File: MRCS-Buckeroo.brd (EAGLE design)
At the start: 69 x 50 mm, 11 parts

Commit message: sent to fab
sent to fab
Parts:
- removed FRAME1: FRAME-LETTER, SparkFun-Aesthetics:CREATIVE_COMMONS
- removed GND: CONNECTOR-M12LOCK, SPCoast:1X12_LOCK
- added OUTPUT-: OUTPUT-, SPCoast:1X12_LOCK
- CON1, CON2: value (none) -> DC PWR
- CON3: value (none) -> output bypass
- CON4: value (none) -> GND BYPASS
- OUTPUT+: value CONNECTOR-M12LOCK -> OUTPUT+
- moved CON3 148.8 mm to (34.3, 44.5)
- moved CON4 144.8 mm to (45.7, 12.7)
- moved U$4 91.4 mm to (35.6, 30.5)
- moved CON2 78.9 mm to (34.3, 10.2)
- moved CON1 55.5 mm to (24.1, 12.7)
- moved U$1 9.25 mm to (40.6, 36.8)
- renumbered OUTPUT to OUTPUT+
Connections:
- net N$1 renamed INPUT+
- net N$2 renamed GND
- net N$4 renamed OUTPUT+
- removed net N$3: CON4.1, GND.1, GND.10, GND.11, GND.12, GND.2, GND.3, GND.4, GND.5, GND.6, GND.7, GND.8, GND.9, U$4.OUT-
- new net OUTPUT-: CON4.1, OUTPUT-.1, OUTPUT-.10, OUTPUT-.11, OUTPUT-.12, OUTPUT-.2, OUTPUT-.3, OUTPUT-.4, OUTPUT-.5, OUTPUT-.6, OUTPUT-.7, OUTPUT-.8, OUTPUT-.9, U$4.OUT-
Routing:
- net INPUT+: track 0.00 -> 78.3 mm
- net OUTPUT-: track 0.00 -> 63.8 mm
- net GND: track 0.00 -> 57.0 mm
- net N$3: track 29.2 -> 0.00 mm
- added copper zone on layer 16, net OUTOUT-
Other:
- board text added: ""Buckeroo" Seth Neumann 20200929"
- board text added: "+ V Jumper"
- board text added: "- V (GND) JUMP"
- board text added: "IN - +"
- board text added: "Output +"
- board text added: "Output -"
- board text removed: "+12V"
- board text removed: "12V"
- board text removed: "CON4"
- board text removed: "Power & Ground Distribution"
- board text removed: "ULK"
- board text removed: "ULK GND +12"
- board text removed: "UnLock"

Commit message: Added 1st pass of documentation
Assembly and Installation Instructions
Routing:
- net OUTPUT-: track 63.8 -> 93.0 mm
- net INPUT+: track 78.3 -> 71.0 mm
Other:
- board text added: ""Buckeroo V1.2" Seth Neumann 20201120"
- board text removed: ""Buckeroo" Seth Neumann 20200929"

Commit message: Added regulator options
Supports MH-Mini-360 bucking converter and 780X TO-220 linear regulators
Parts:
- added C1: 150uF@50, SPCoast:E5-10.5
- added C2: 1.0uF@50, SPCoast:C-PTH-0.100
- added C3: 10uF@50, SPCoast:C-PTH-0.100
- added MH-MINI-360: MH-MINI-360, MH-MINI-360:MH-MINI-360
- added VR1: 780X, SPCoast:TO-220-RA
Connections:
- net GND: now also C1.-, C2.2, MH-MINI-360.IN-
- net INPUT+: now also C1.+, C2.1, MH-MINI-360.INN+, VR1.IN
- net OUTPUT+: now also C3.1, MH-MINI-360.OUTT+, VR1.OUT
- net OUTPUT-: now also C3.2, MH-MINI-360.OUT-, VR1.GND
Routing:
- net OUTPUT-: track 93.0 -> 140.9 mm
- net GND: track 57.0 -> 96.4 mm
- net INPUT+: track 71.0 -> 93.8 mm
- net OUTPUT+: track 56.8 -> 79.3 mm
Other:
- board text added: ""Buckeroo V1.3" Seth Neumann 20221113"
- board text added: "- In +"
- board text added: "- Out +"
- board text removed: ""Buckeroo V1.2" Seth Neumann 20201120"

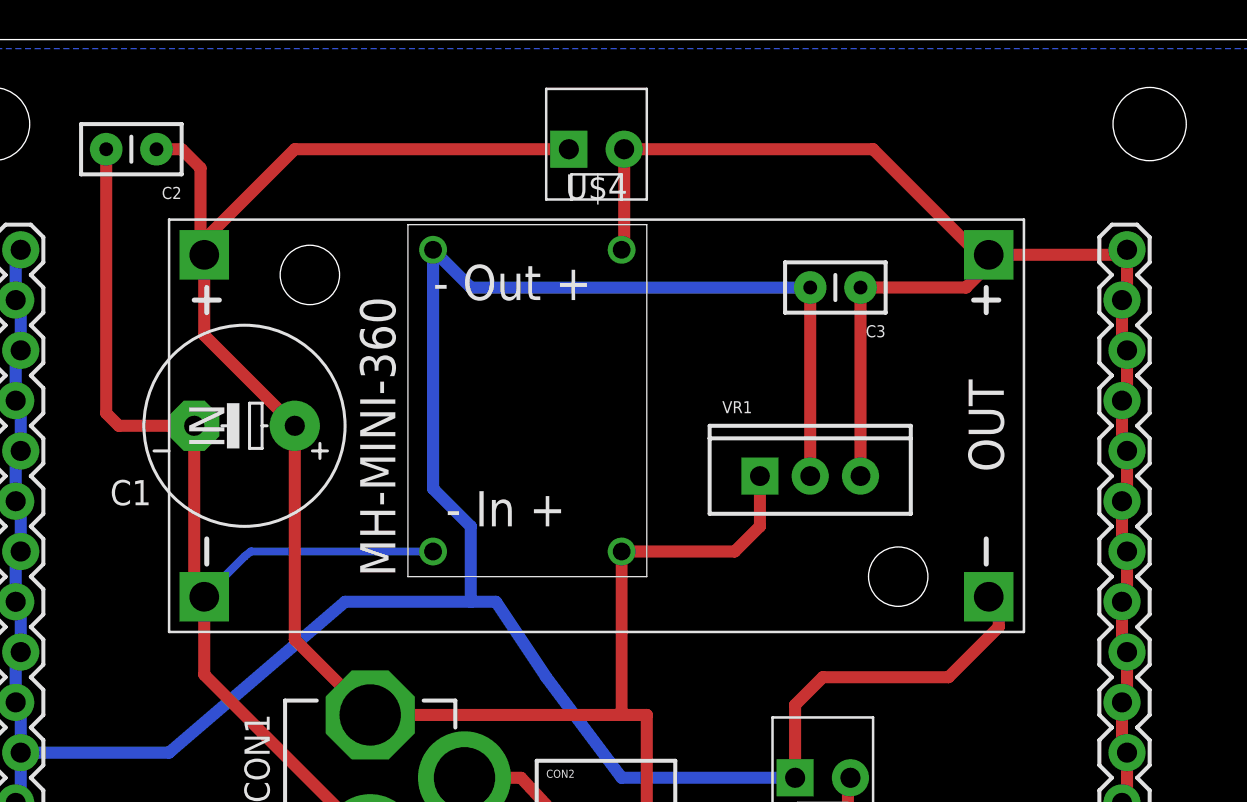
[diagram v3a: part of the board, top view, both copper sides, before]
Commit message: Release 3 sent out for fab
These include the mini bucker and an updown bucker as well as the pads for 780X TO220 packages. These need to be tested before panelization.
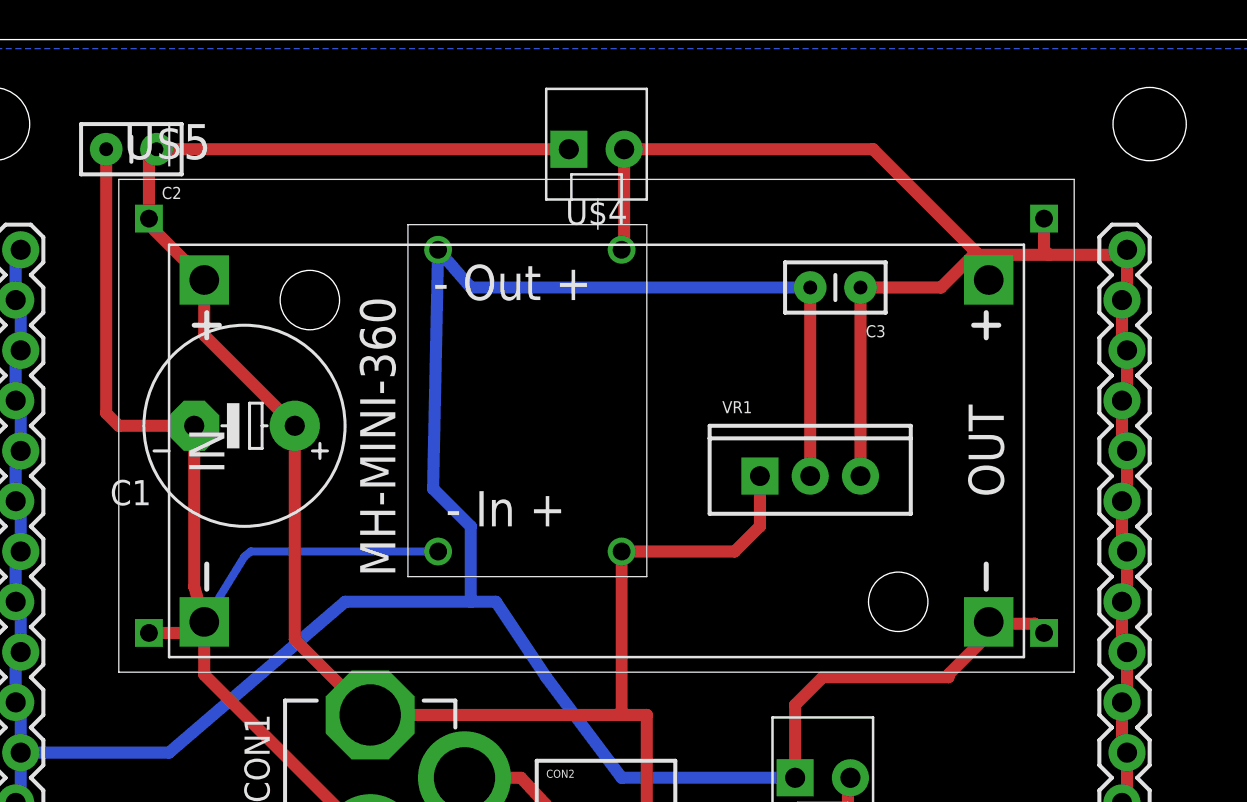
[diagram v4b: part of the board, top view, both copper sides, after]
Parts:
- added U$5: XL6009BOARD, MRCS:XL6009_BOARD
- MH-MINI-360: device MH-MINI-360:MH-MINI-360 -> MRCS:MH-MINI-360
- moved U$4 1.27 mm to (35.6, 29.2)
- moved U$1 1.27 mm to (40.6, 35.6)
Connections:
- net GND: now also U$5.IN-
- net INPUT+: now also U$5.IN+
- net OUTPUT+: now also U$5.OUT+
- net OUTPUT-: now also U$5.OUT-
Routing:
- net GND: track 96.4 -> 100.4 mm
- net OUTPUT+: track 79.3 -> 81.7 mm
- net OUTPUT-: track 140.9 -> 141.7 mm
- net INPUT+: track 93.8 -> 93.1 mm
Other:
- board text added: ""Buckeroo V1.4" Seth Neumann 20230102"
- board text removed: ""Buckeroo V1.3" Seth Neumann 20221113"
